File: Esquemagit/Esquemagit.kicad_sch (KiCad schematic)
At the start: 20 parts, among them U1 LMV321, U5 ESP32-WROOM-32

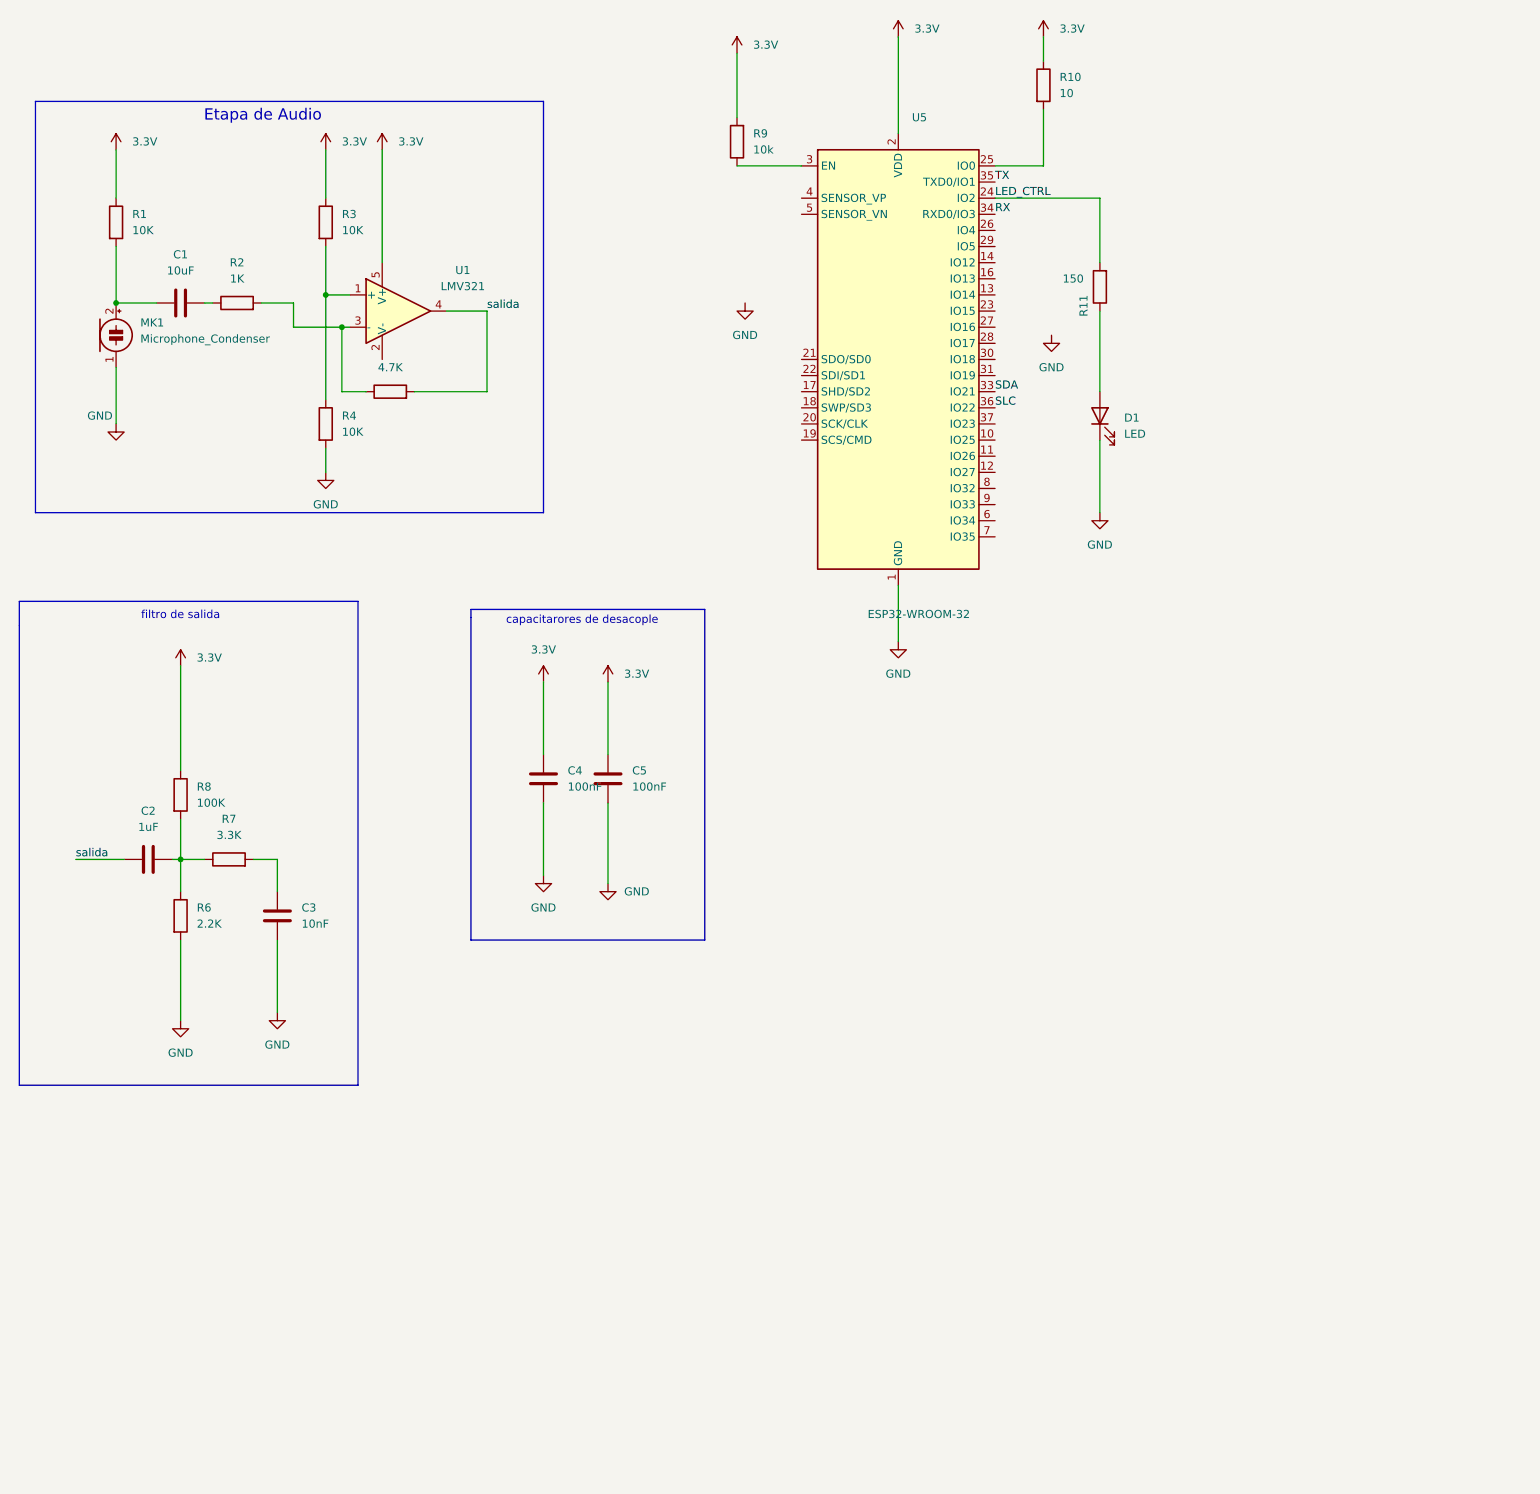
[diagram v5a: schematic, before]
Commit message: feat: huellas asignadas,botones de reset,usb-regulador,
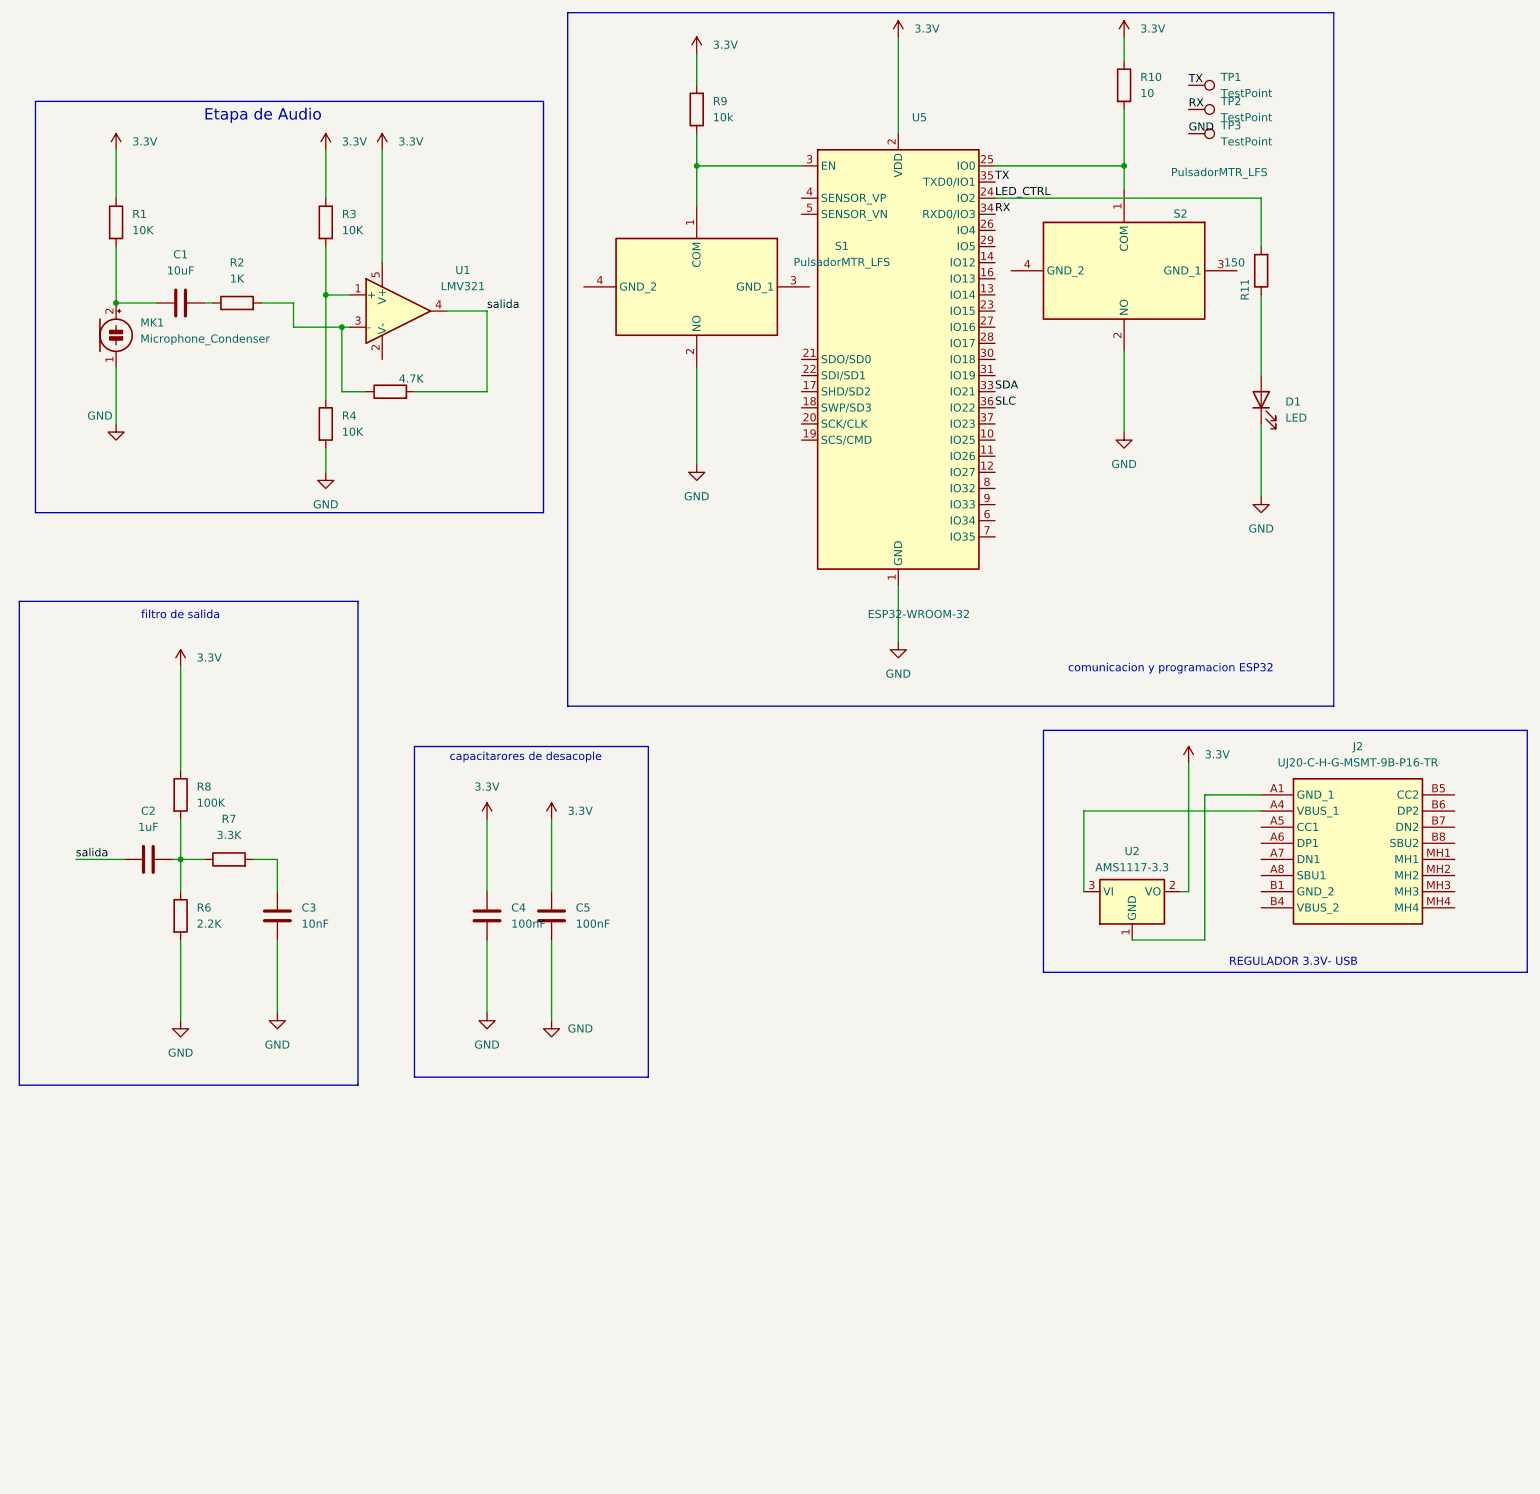
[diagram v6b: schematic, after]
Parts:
- added J2: UJ20-C-H-G-MSMT-9B-P16-TR, UJ20CHGMSMT9BP16TR, symbol UJ20-C-H-G-MSMT-9B-P16-TR:UJ20-C-H-G-MSMT-9B-P16-TR
- added S1, S2: PulsadorMTR_LFS, Button_Switch_SMD:SW_DIP_SPSTx02_Slide_6.7x6.64mm_W6.73mm_P2.54mm_LowProfile_JPin, symbol pulsador:PulsadorMTR_LFS
- added TP1, TP2, TP3: TestPoint, TestPoint:TestPoint_Pad_D1.5mm, symbol Connector:TestPoint
- added U2: AMS1117-3.3, Package_TO_SOT_SMD:SOT-223-3_TabPin2, symbol Regulator_Linear:AMS1117-3.3
- C4: footprint Capacitor_THT:C_Disc_D5.0mm_W2.5mm_P5.00mm -> Capacitor_SMD:C_0805_2012Metric
- R3: footprint Resistor_THT:R_Axial_DIN0207_L6.3mm_D2.5mm_P7.62mm_Horizontal -> Resistor_SMD:R_0805_2012Metric
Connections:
- net 3.3V: now also U2.2 (VO)
- net GND: now also S1.2 (NO), S2.2 (NO), TP3.1
- net RX: now also TP2.1
- net TX: now also TP1.1
- net at R9.1, U5.3 (EN): now also S1.1 (COM)
- net at R10.2, U5.25 (IO0): now also S2.1 (COM)
- new net: J2.A1 (GND_1), U2.1 (GND)
- new net: J2.A4 (VBUS_1), U2.3 (VI)
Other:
- note added: "REGULADOR 3.3V- USB"
- note added: "comunicacion y programacion ESP32"
- moved on the sheet: C4, C5, D1, R10, R11, R9

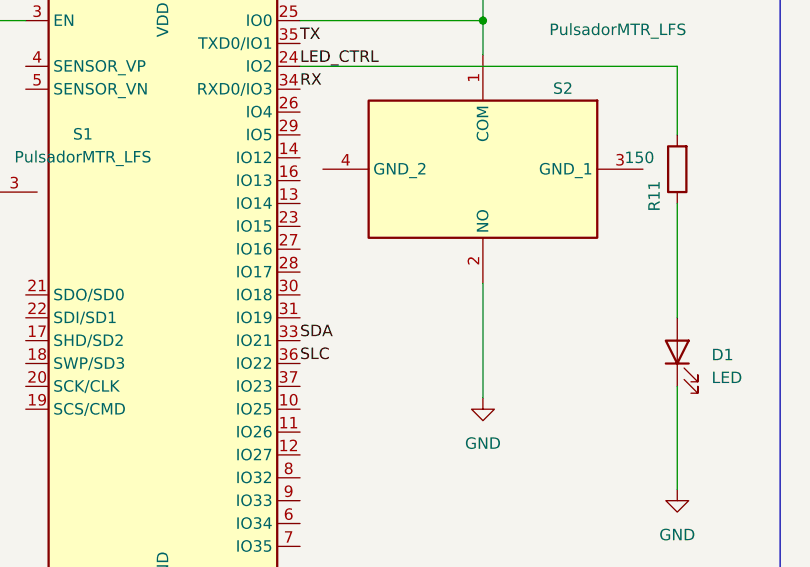
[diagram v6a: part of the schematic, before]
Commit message: Realice ajustes de componenetes en pcb y ademas cableado de pistas
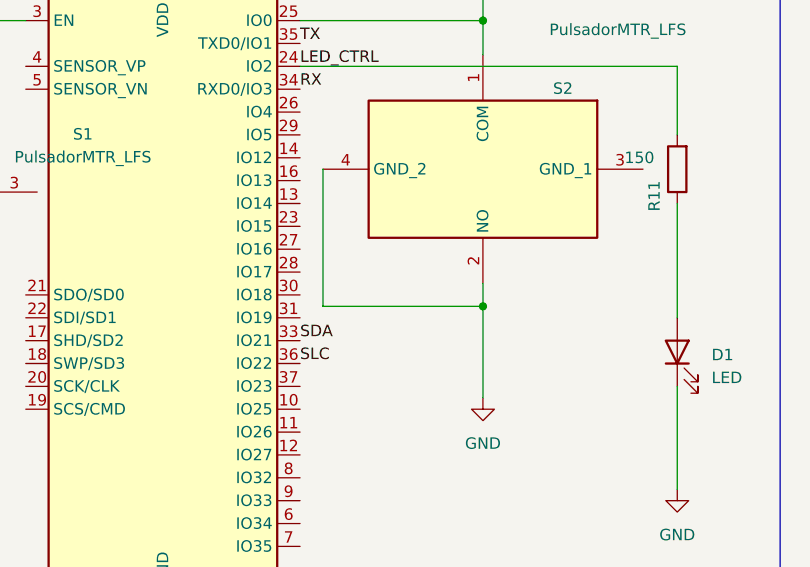
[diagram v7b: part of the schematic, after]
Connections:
- net GND: now also S2.4 (GND_2)
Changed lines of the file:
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@@
+	)
+	(junction
+		(at 203.2 69.85)
+		(diameter 0)
+		(color 0 0 0 0)
 	)
 	(junction
@@
 	(wire
 		(pts
+			(xy 203.2 69.85) (xy 203.2 80.01)
+		)
+		(stroke
+			(width 0)
+			(type default)
+		)
+	)
+	(wire
+		(pts
 			(xy 44.45 59.69) (xy 50.8 59.69)
 		)
@@
 	(wire
 		(pts
+			(xy 185.42 69.85) (xy 203.2 69.85)
+		)
+		(stroke
+			(width 0)
+			(type default)
+		)
+	)
+	(wire
+		(pts
 			(xy 69.85 160.02) (xy 69.85 171.45)
 		)
@@
 		)
 	)
+	(wire
+		(pts
+			(xy 185.42 54.61) (xy 185.42 69.85)
+		)
+		(stroke
+			(width 0)
+			(type default)
+		)
+	)
 	(polyline
 		(pts
@@
 	(wire
 		(pts
-			(xy 203.2 67.31) (xy 203.2 80.01)
-		)
-		(stroke
+			(xy 203.2 67.31) (xy 203.2 69.85)
+		)
+		(stroke
